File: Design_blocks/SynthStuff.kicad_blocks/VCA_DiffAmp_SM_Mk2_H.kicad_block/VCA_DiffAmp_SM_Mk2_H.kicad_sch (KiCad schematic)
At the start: 20 parts, among them J1 Conn_01x02, J2 Conn_01x04, Q1 BC548, Q2 BC548, U1 TL072

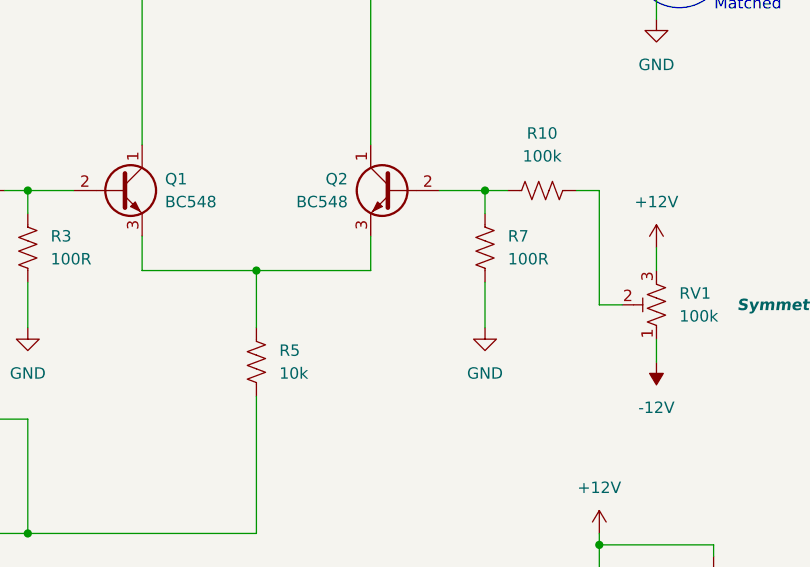
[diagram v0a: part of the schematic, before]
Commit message: VCA minor updates after Mk2 submodule PCB design
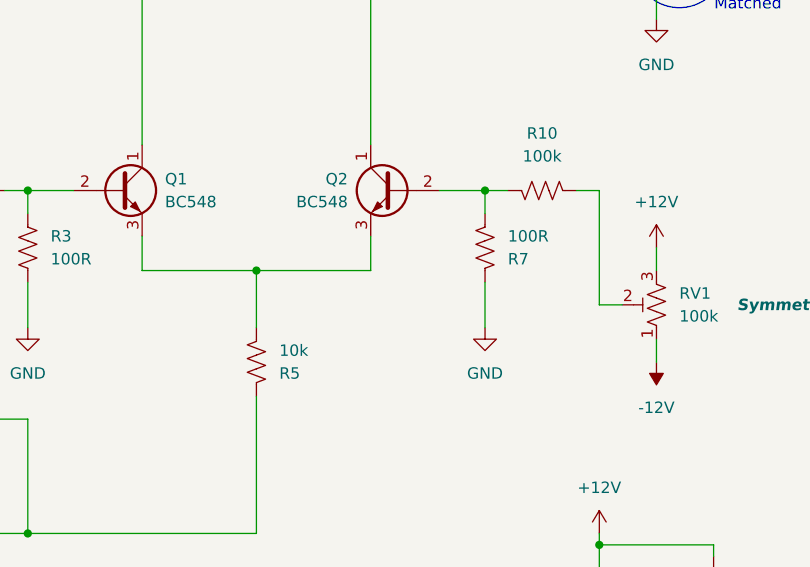
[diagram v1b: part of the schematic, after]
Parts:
- R1, R10, R11, R12, R2, R3, R4, R5, R6, R7, R8, R9: footprint Resistor_THT:R_Axial_DIN0207_L6.3mm_D2.5mm_P7.62mm_Horizontal -> Resistor_THT:R_Axial_DIN0207_L6.3mm_D2.5mm_P2.54mm_Vertical
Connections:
- net GND: now also R7.2; no longer R7.1
- net at R1.2, U1.1: now also R5.2; no longer R5.1
- net at Q1.3 (E), Q2.3 (E): now also R5.1; no longer R5.2
- net at R10.1: now also Q2.2 (B), R7.1; no longer RV1.2
- new net: R10.2, RV1.2
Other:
- moved on the sheet: R10, R5, R7
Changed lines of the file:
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@@
 		)
 	)
-	(hierarchical_label "Signal_In"
+	(hierarchical_label "CV_Mix_In"
 		(shape input)
-		(at 125.73 88.9 180)
+		(at 107.95 124.46 180)
 		(effects
 			(font
@@
 		)
 	)
-	(hierarchical_label "CV_Mix_In"
+	(hierarchical_label "Signal_In"
 		(shape input)
-		(at 107.95 124.46 180)
+		(at 127 151.13 180)
 		(effects
 			(font
@@
 		)
 	)
-	(hierarchical_label "CV_Mix_In"
-		(shape input)
-		(at 127 153.67 180)
+	(hierarchical_label "Signal_Out"
+		(shape output)
+		(at 241.3 50.8 0)
 		(effects
 			(font
 				(size 1.27 1.27)
 			)
-			(justify right)
+			(justify left)
 		)
 	)
-	(hierarchical_label "Signal_In"
+	(hierarchical_label "CV_Mix_In"
 		(shape input)
-		(at 127 151.13 180)
+		(at 127 153.67 180)
 		(effects
 			(font
@@
 		)
 	)
-	(hierarchical_label "Signal_Out"
-		(shape output)
-		(at 241.3 50.8 0)
+	(hierarchical_label "Signal_In"
+		(shape input)
+		(at 125.73 88.9 180)
 		(effects
 			(font
 				(size 1.27 1.27)
 			)
-			(justify left)
+			(justify right)
 		)
 	)
@@
 			)
 		)
-		(property "Footprint" "Resistor_THT:R_Axial_DIN0207_L6.3mm_D2.5mm_P7.62mm_Horizontal"
+		(property "Footprint" "Resistor_THT:R_Axial_DIN0207_L6.3mm_D2.5mm_P2.54mm_Vertical"
 			(at 221.996 39.116 90)
 			(hide yes)
@@
 			)
 		)
-		(property "Footprint" "Resistor_THT:R_Axial_DIN0207_L6.3mm_D2.5mm_P7.62mm_Horizontal"
+		(property "Footprint" "Resistor_THT:R_Axial_DIN0207_L6.3mm_D2.5mm_P2.54mm_Vertical"
 			(at 133.096 89.916 90)
 			(hide yes)
@@
 			)
 		)
-		(property "Footprint" "Resistor_THT:R_Axial_DIN0207_L6.3mm_D2.5mm_P7.62mm_Horizontal"
+		(property "Footprint" "Resistor_THT:R_Axial_DIN0207_L6.3mm_D2.5mm_P2.54mm_Vertical"
 			(at 125.984 113.284 90)
 			(hide yes)
@@
 			)
 		)
-		(property "Footprint" "Resistor_THT:R_Axial_DIN0207_L6.3mm_D2.5mm_P7.62mm_Horizontal"
+		(property "Footprint" "Resistor_THT:R_Axial_DIN0207_L6.3mm_D2.5mm_P2.54mm_Vertical"
 			(at 138.684 94.996 90)
 			(hide yes)
@@
 			)
 		)
-		(property "Footprint" "Resistor_THT:R_Axial_DIN0207_L6.3mm_D2.5mm_P7.62mm_Horizontal"
+		(property "Footprint" "Resistor_THT:R_Axial_DIN0207_L6.3mm_D2.5mm_P2.54mm_Vertical"
 			(at 196.596 56.134 90)
 			(hide yes)
@@
 			)
 		)
-		(property "Footprint" "Resistor_THT:R_Axial_DIN0207_L6.3mm_D2.5mm_P7.62mm_Horizontal"
+		(property "Footprint" "Resistor_THT:R_Axial_DIN0207_L6.3mm_D2.5mm_P2.54mm_Vertical"
 			(at 178.816 31.496 90)
 			(hide yes)
@@
 	(symbol
 		(lib_id "Device:R_US")
-		(at 165.1 107.95 180)
+		(at 165.1 107.95 0)
+		(mirror y)
 		(unit 1)
 		(body_style 1)
@@
 		(in_pos_files yes)
 		(dnp no)
-		(fields_autoplaced yes)
 		(property "Reference" "R5"
-			(at 167.64 106.6799 0)
+			(at 167.64 109.2201 0)
 			(show_name no)
 			(do_not_autoplace no)
@@
 		)
 		(property "Value" "10k"
-			(at 167.64 109.2199 0)
+			(at 167.64 106.6801 0)
 			(show_name no)
 			(do_not_autoplace no)
@@
 			)
 		)
-		(property "Footprint" "Resistor_THT:R_Axial_DIN0207_L6.3mm_D2.5mm_P7.62mm_Horizontal"
-			(at 164.084 107.696 90)
+		(property "Footprint" "Resistor_THT:R_Axial_DIN0207_L6.3mm_D2.5mm_P2.54mm_Vertical"
+			(at 164.084 108.204 90)
 			(hide yes)
 			(show_name no)
@@
 	(symbol
 		(lib_id "Device:R_US")
-		(at 190.5 95.25 180)
+		(at 190.5 95.25 0)
+		(mirror y)
 		(unit 1)
 		(body_style 1)
@@
 		(in_pos_files yes)
 		(dnp no)
-		(fields_autoplaced yes)
 		(property "Reference" "R7"
-			(at 193.04 93.9799 0)
+			(at 193.04 96.5201 0)
 			(show_name no)
 			(do_not_autoplace no)
@@
 		)
 		(property "Value" "100R"
-			(at 193.04 96.5199 0)
+			(at 193.04 93.9801 0)
 			(show_name no)
 			(do_not_autoplace no)
@@
 			)
 		)
-		(property "Footprint" "Resistor_THT:R_Axial_DIN0207_L6.3mm_D2.5mm_P7.62mm_Horizontal"
-			(at 189.484 94.996 90)
+		(property "Footprint" "Resistor_THT:R_Axial_DIN0207_L6.3mm_D2.5mm_P2.54mm_Vertical"
+			(at 189.484 95.504 90)
 			(hide yes)
 			(show_name no)
@@
 	(symbol
 		(lib_id "Device:R_US")
-		(at 196.85 88.9 270)
+		(at 196.85 88.9 90)
+		(mirror x)
 		(unit 1)
 		(body_style 1)
@@
 		(in_pos_files yes)
 		(dnp no)
-		(fields_autoplaced yes)
 		(property "Reference" "R10"
 			(at 196.85 82.55 90)
@@
 			)
 		)
-		(property "Footprint" "Resistor_THT:R_Axial_DIN0207_L6.3mm_D2.5mm_P7.62mm_Horizontal"
-			(at 196.596 89.916 90)
+		(property "Footprint" "Resistor_THT:R_Axial_DIN0207_L6.3mm_D2.5mm_P2.54mm_Vertical"
+			(at 197.104 89.916 90)
 			(hide yes)
 			(show_name no)
@@
 			)
 		)
-		(property "Footprint" "Resistor_THT:R_Axial_DIN0207_L6.3mm_D2.5mm_P7.62mm_Horizontal"
+		(property "Footprint" "Resistor_THT:R_Axial_DIN0207_L6.3mm_D2.5mm_P2.54mm_Vertical"
 			(at 210.566 63.754 90)
 			(hide yes)
@@
 			)
 		)
-		(property "Footprint" "Resistor_THT:R_Axial_DIN0207_L6.3mm_D2.5mm_P7.62mm_Horizontal"
+		(property "Footprint" "Resistor_THT:R_Axial_DIN0207_L6.3mm_D2.5mm_P2.54mm_Vertical"
 			(at 196.596 45.466 90)
 			(hide yes)
@@
 			)
 		)
-		(property "Footprint" "Resistor_THT:R_Axial_DIN0207_L6.3mm_D2.5mm_P7.62mm_Horizontal"
+		(property "Footprint" "Resistor_THT:R_Axial_DIN0207_L6.3mm_D2.5mm_P2.54mm_Vertical"
 			(at 151.384 31.496 90)
 			(hide yes)

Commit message: Updated VCA Mk2 design blocks
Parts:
- added C5: 33pF, Capacitor_THT:C_Disc_D3.4mm_W2.1mm_P2.50mm, symbol Device:C
- added JP1, JP2: SolderJumper_3_Open, Jumper:SolderJumper-3_P1.3mm_Open_RoundedPad1.0x1.5mm_NumberLabels, symbol Jumper:SolderJumper_3_Open
- added TP1: TestPoint_Probe, TestPoint:TestPoint_THTPad_D1.0mm_Drill0.5mm, symbol Connector:TestPoint_Probe
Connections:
- net Signal_Out: now also C5.2, TP1.1
- net at R12.2, R8.1, U1.6 (-): now also C5.1
- net at Q2.1 (C), R6.1: now also JP1.1 (A), JP2.3 (B); no longer R9.2
- net at Q1.1 (C), R4.1: now also JP1.3 (B), JP2.1 (A); no longer R8.2
- new net: JP2.2 (C), R9.2
- new net: JP1.2 (C), R8.2
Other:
- note removed: "Matched"
- moved on the sheet: R8
